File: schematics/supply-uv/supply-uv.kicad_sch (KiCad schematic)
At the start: 5 parts, among them J1 Conn_01x02_Pin, J3 Conn_01x01_Pin

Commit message: Found and fixed issues in schematics.
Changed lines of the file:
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@@
     (stroke (width 0) (type default))
+  )
+  (text_box "Known issues:\n- wrong place for R1-R3 (not a problem)\n- probably cooler required on QP1 (THIS IS PROBLEM!)\n- bad board layout near PFC GND"
+    (at 212.09 16.51 0) (size 68.58 48.26)
+    (stroke (width 0) (type default))
+    (fill (type none))
+    (effects (font (size 1.27 1.27)) (justify left top))
   )
   (text "Holes on board#2" (at 74.93 156.21 0)

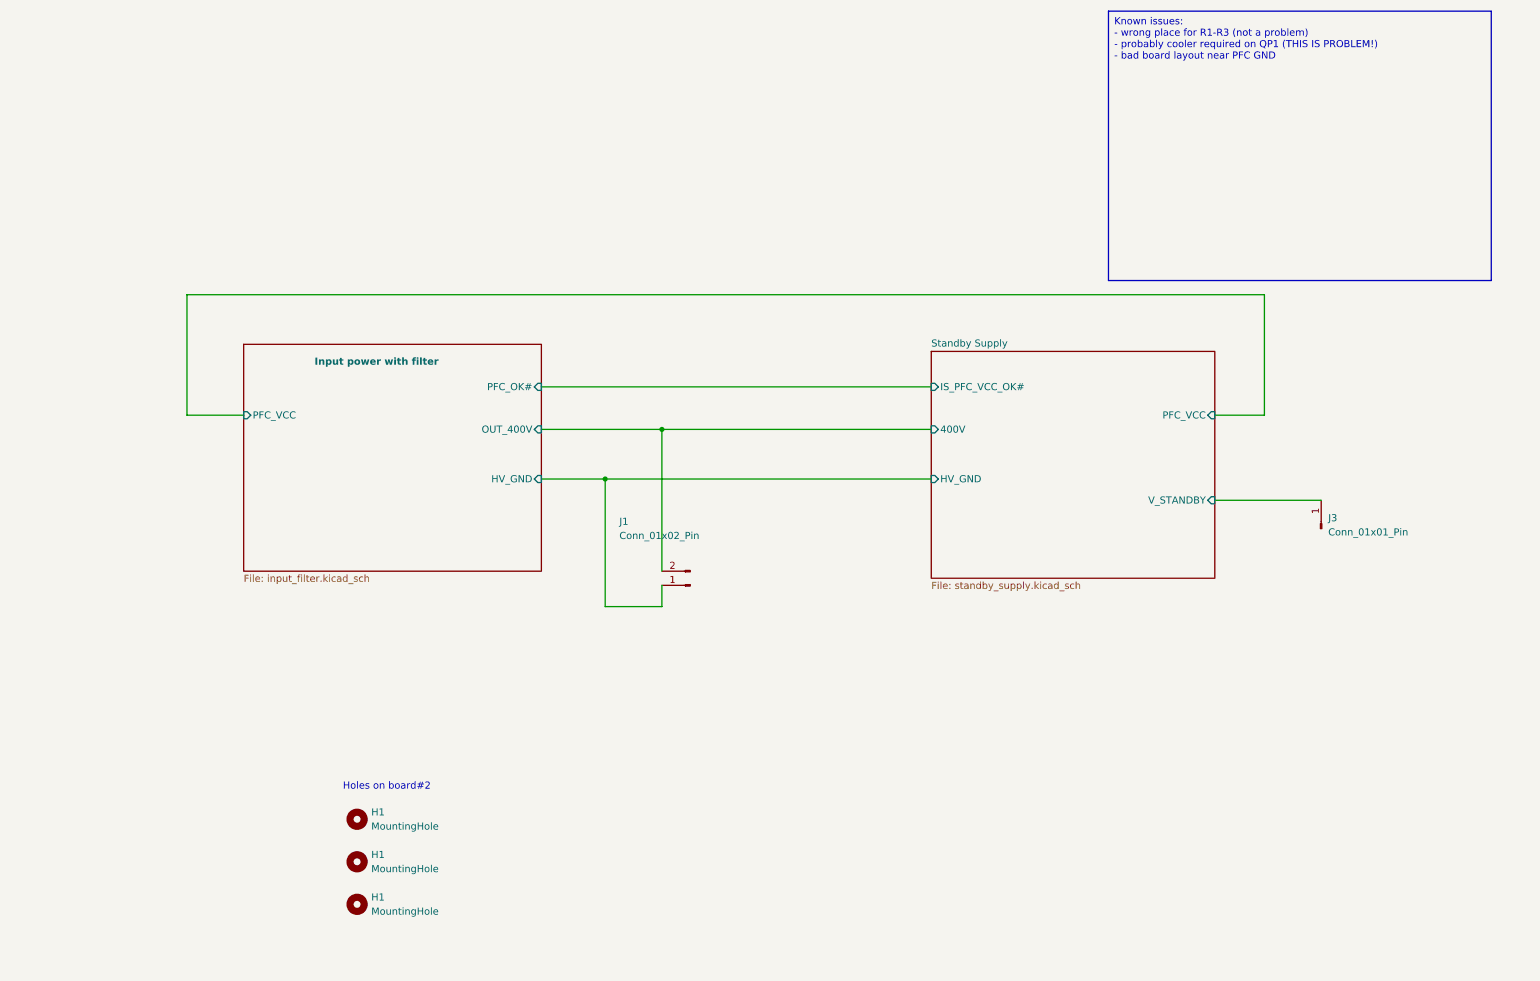
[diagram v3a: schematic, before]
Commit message: first schema version for board-uv
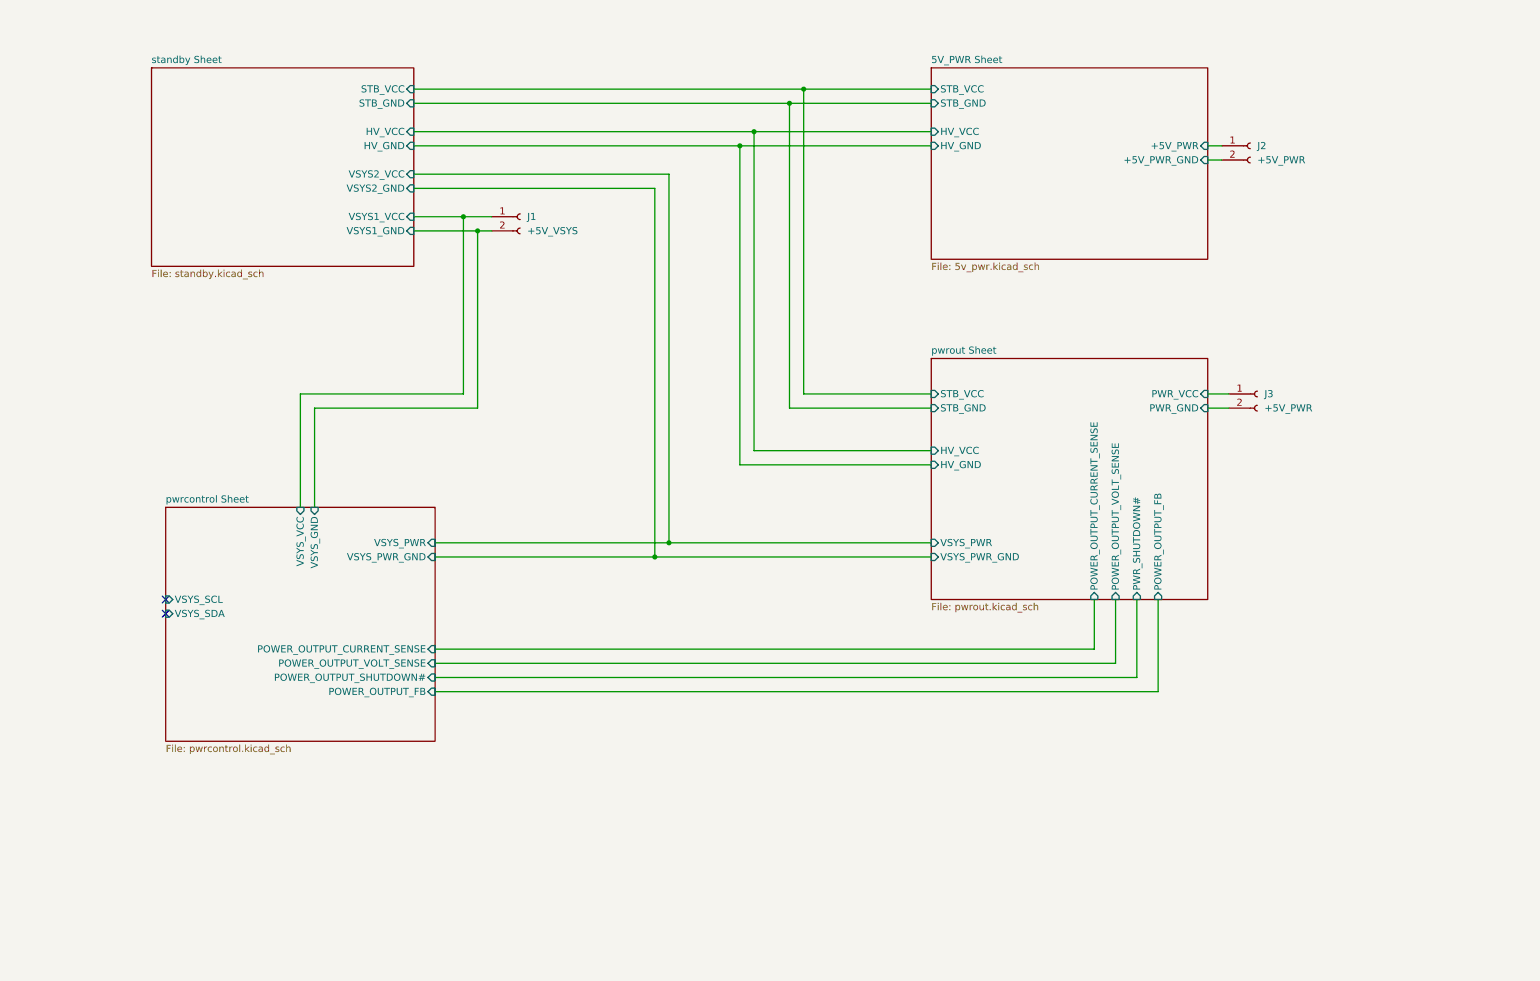
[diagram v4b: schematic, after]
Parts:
- removed H1 (x3): MountingHole, MountingHole:MountingHole_2.2mm_M2, symbol Mechanical:MountingHole
- removed J1: Conn_01x02_Pin, Connector_Wire:SolderWire-1.5sqmm_1x02_P6mm_D1.7mm_OD3mm, symbol Connector:Conn_01x02_Pin
- removed J3: Conn_01x01_Pin, Connector_Wire:SolderWire-1.5sqmm_1x01_D1.7mm_OD3.9mm, symbol Connector:Conn_01x01_Pin
- added J1: +5V_VSYS, symbol Connector:Conn_01x02_Socket
- added J2, J3: +5V_PWR, symbol Connector:Conn_01x02_Socket
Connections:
- new net 5V_PWR Sheet/+5V_PWR: J2.1 (Pin_1)
- new net 5V_PWR Sheet/+5V_PWR_GND: J2.2 (Pin_2)
- new net pwrcontrol Sheet/VSYS_GND: J1.2 (Pin_2)
- new net pwrcontrol Sheet/VSYS_VCC: J1.1 (Pin_1)
- new net pwrout Sheet/PWR_GND: J3.2 (Pin_2)
- new net pwrout Sheet/PWR_VCC: J3.1 (Pin_1)
- no-connect marks 0 -> 2
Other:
- removed sheet Input power with filter
- removed sheet Standby Supply
- added sheet 5V_PWR Sheet (5v_pwr.kicad_sch)
- added sheet pwrcontrol Sheet (pwrcontrol.kicad_sch)
- added sheet pwrout Sheet (pwrout.kicad_sch)
- added sheet standby Sheet (standby.kicad_sch)
- note removed: "Holes on board#2"

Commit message: Board#1 schematics rewrited
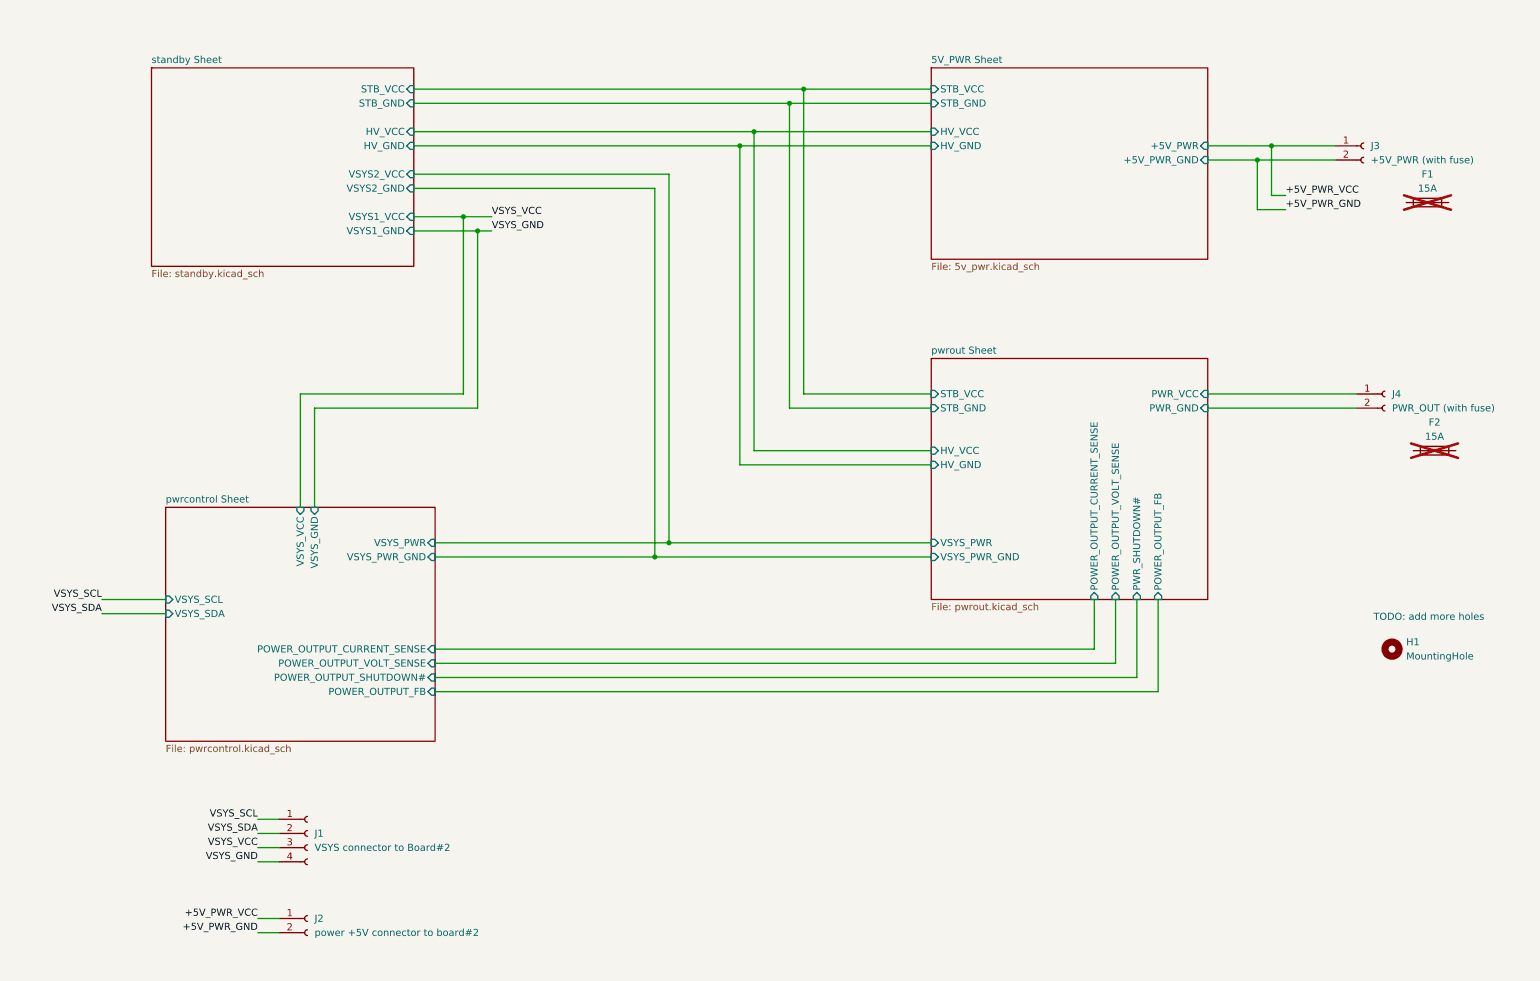
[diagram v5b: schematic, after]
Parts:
- removed J1: +5V_VSYS, symbol Connector:Conn_01x02_Socket
- removed J3: +5V_PWR, symbol Connector:Conn_01x02_Socket
- added F1, F2: 15A, symbol Device:Fuse
- added H1: MountingHole, MountingHole:MountingHole_2.2mm_M2, symbol Mechanical:MountingHole
- added J1: VSYS connector to Board#2, Connector_JST:JST_XH_B4B-XH-A_1x04_P2.50mm_Vertical, symbol Connector:Conn_01x04_Socket
- added J2: power +5V connector to board#2, Connector_Wire:SolderWire-1.5sqmm_1x02_P6mm_D1.7mm_OD3mm, symbol Connector:Conn_01x02_Socket
- added J4: PWR_OUT (with fuse), Connector_Wire:SolderWire-1.5sqmm_1x02_P6mm_D1.7mm_OD3mm, symbol Connector:Conn_01x02_Socket
- J3: renamed from J2; value +5V_PWR -> +5V_PWR (with fuse); footprint (none) -> Connector_Wire:SolderWire-1.5sqmm_1x02_P6mm_D1.7mm_OD3mm
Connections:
- net pwrout Sheet/PWR_GND: now also J4.2 (Pin_2)
- net pwrout Sheet/PWR_VCC: now also J4.1 (Pin_1)
- net 5V_PWR Sheet/+5V_PWR renamed +5V_PWR_VCC
- net +5V_PWR_VCC: now also J2.1 (Pin_1)
- net 5V_PWR Sheet/+5V_PWR_GND renamed +5V_PWR_GND
- net +5V_PWR_GND: now also J2.2 (Pin_2)
- new net VSYS_GND: J1.4 (Pin_4)
- new net VSYS_SCL: J1.1 (Pin_1)
- new net VSYS_SDA: J1.2 (Pin_2)
- new net VSYS_VCC: J1.3 (Pin_3)
- no-connect marks 2 -> 0
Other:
- note added: "TODO: add more holes"
- moved on the sheet: J3

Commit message: added some protection logic
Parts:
- added C1, C2: 100 nF, Capacitor_SMD:C_0603_1608Metric, symbol Device:C
- added U1: ISO1540, Package_SO:SOIC-8_3.9x4.9mm_P1.27mm, symbol Isolator:ISO1540
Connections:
- net VSYS_GND: now also C2.2, U1.5 (GND2)
- net VSYS_SCL: now also U1.6 (SCL2)
- net VSYS_SDA: now also U1.7 (SDA2)
- net VSYS_VCC: now also C2.1, U1.8 (VCC2)
- new net VSYS_PWR_GND: C1.2, U1.4 (GND1)
- new net VSYS_PWR_SCL: U1.3 (SCL1)
- new net VSYS_PWR_SDA: U1.2 (SDA1)
- new net VSYS_PWR_VCC: C1.1, U1.1 (VCC1)
- no-connect marks 0 -> 4
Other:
- sheet pwrcontrol Sheet ports: added SCL, SDA, VSYS_PWR_VCC; removed VSYS_GND, VSYS_PWR, VSYS_SCL, VSYS_SDA, VSYS_VCC
- sheet pwrout Sheet ports: added VSYS_PWR_VCC; removed VSYS_PWR
- moved on the sheet: J1, J2

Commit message: start board#1 tracing
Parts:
- added JP4: 5V_EN, Jumper:SolderJumper-2_P1.3mm_Open_TrianglePad1.0x1.5mm, symbol Jumper:SolderJumper_2_Open
- added JP5: PWR_EN, Jumper:SolderJumper-2_P1.3mm_Open_TrianglePad1.0x1.5mm, symbol Jumper:SolderJumper_2_Open
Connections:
- net 5V_PWR Sheet/STB_VCC: now also JP4.2 (B)
- new net pwrout Sheet/STB_VCC: JP5.2 (B)
- new net standby Sheet/STB_VCC: JP4.1 (A), JP5.1 (A)
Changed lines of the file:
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@@
 	)
 	(junction
-		(at 157.48 30.48)
+		(at 162.56 30.48)
 		(diameter 0)
 		(color 0 0 0 0)
@@
 	(wire
 		(pts
+			(xy 130.81 167.64) (xy 134.62 167.64)
+		)
+		(stroke
+			(width 0)
+			(type default)
+		)
+	)
+	(wire
+		(pts
 			(xy 148.59 38.1) (xy 180.34 38.1)
 		)
@@
 	(wire
 		(pts
+			(xy 130.81 165.1) (xy 134.62 165.1)
+		)
+		(stroke
+			(width 0)
+			(type default)
+		)
+	)
+	(wire
+		(pts
 			(xy 91.44 130.81) (xy 209.55 130.81)
 		)
@@
 	(wire
 		(pts
-			(xy 180.34 85.09) (xy 157.48 85.09)
+			(xy 176.53 85.09) (xy 180.34 85.09)
 		)
 		(stroke
@@
 	(wire
 		(pts
-			(xy 130.81 167.64) (xy 134.62 167.64)
-		)
-		(stroke
-			(width 0)
-			(type default)
-		)
-	)
-	(wire
-		(pts
 			(xy 130.81 170.18) (xy 134.62 170.18)
 		)
@@
 	(wire
 		(pts
-			(xy 157.48 30.48) (xy 180.34 30.48)
-		)
-		(stroke
-			(width 0)
-			(type default)
-		)
-	)
-	(wire
-		(pts
 			(xy 87.63 33.02) (xy 154.94 33.02)
 		)
@@
 	(wire
 		(pts
-			(xy 130.81 165.1) (xy 134.62 165.1)
-		)
-		(stroke
-			(width 0)
-			(type default)
-		)
-	)
-	(wire
-		(pts
 			(xy 213.36 133.35) (xy 213.36 121.92)
 		)
@@
 	(wire
 		(pts
+			(xy 162.56 30.48) (xy 167.64 30.48)
+		)
+		(stroke
+			(width 0)
+			(type default)
+		)
+	)
+	(wire
+		(pts
 			(xy 59.69 180.34) (xy 64.77 180.34)
 		)
@@
 	(wire
 		(pts
+			(xy 162.56 85.09) (xy 168.91 85.09)
+		)
+		(stroke
+			(width 0)
+			(type default)
+		)
+	)
+	(wire
+		(pts
 			(xy 238.76 52.07) (xy 238.76 43.18)
 		)
@@
 	(wire
 		(pts
-			(xy 87.63 30.48) (xy 157.48 30.48)
+			(xy 87.63 30.48) (xy 162.56 30.48)
 		)
 		(stroke
@@
 	(wire
 		(pts
-			(xy 157.48 85.09) (xy 157.48 30.48)
+			(xy 175.26 30.48) (xy 180.34 30.48)
+		)
+		(stroke
+			(width 0)
+			(type default)
+		)
+	)
+	(wire
+		(pts
+			(xy 162.56 85.09) (xy 162.56 30.48)
 		)
 		(stroke
@@
 			)
 			(justify right bottom)
+		)
+	)
+	(symbol
+		(lib_id "Jumper:SolderJumper_2_Open")
+		(at 171.45 30.48 0)
+		(unit 1)
+		(exclude_from_sim yes)
+		(in_bom no)
+		(on_board yes)
+		(dnp no)
+		(fields_autoplaced yes)
+		(property "Reference" "JP4"
+			(at 171.45 24.13 0)
+			(effects
+				(font
+					(size 1.27 1.27)
+				)
+			)
+		)
+		(property "Value" "5V_EN"
+			(at 171.45 26.67 0)
+			(effects
+				(font
+					(size 1.27 1.27)
+				)
+			)
+		)
+		(property "Footprint" "Jumper:SolderJumper-2_P1.3mm_Open_TrianglePad1.0x1.5mm"
+			(at 171.45 30.48 0)
+			(effects
+				(font
+					(size 1.27 1.27)
+				)
+				(hide yes)
+			)
+		)
+		(property "Datasheet" "~"
+			(at 171.45 30.48 0)
+			(effects
+				(font
+					(size 1.27 1.27)
+				)
+				(hide yes)
+			)
+		)
+		(property "Description" "Solder Jumper, 2-pole, open"
+			(at 171.45 30.48 0)
+			(effects
+				(font
+					(size 1.27 1.27)
+				)
+				(hide yes)
+			)
+		)
+		(pin "1"
+		)
+		(pin "2"
+		)
+		(instances
+			(project ""
+				(path "/ef40850c-d0bf-4cba-961b-9aba418f8e73"
+					(reference "JP4")
+					(unit 1)
+				)
+			)
 		)
 	)
@@
 					(unit 1)
 				)
+			)
+		)
+	)
+	(symbol
+		(lib_id "Jumper:SolderJumper_2_Open")
+		(at 172.72 85.09 0)
+		(unit 1)
+		(exclude_from_sim yes)
+		(in_bom no)
+		(on_board yes)
+		(dnp no)
+		(fields_autoplaced yes)
+		(property "Reference" "JP5"
+			(at 172.72 78.74 0)
+			(effects
+				(font
+					(size 1.27 1.27)
+				)
+			)
+		)
+		(property "Value" "PWR_EN"
+			(at 172.72 81.28 0)
+			(effects
+				(font
+					(size 1.27 1.27)
+				)
+			)
+		)
+		(property "Footprint" "Jumper:SolderJumper-2_P1.3mm_Open_TrianglePad1.0x1.5mm"
+			(at 172.72 85.09 0)
+			(effects
+				(font
+					(size 1.27 1.27)
+				)
+				(hide yes)
+			)
+		)
+		(property "Datasheet" "~"
+			(at 172.72 85.09 0)
+			(effects
+				(font
+					(size 1.27 1.27)
+				)
+				(hide yes)
+			)
+		)
+		(property "Description" "Solder Jumper, 2-pole, open"
+			(at 172.72 85.09 0)
+			(effects
+				(font
+					(size 1.27 1.27)
+				)
+				(hide yes)
+			)
+		)
+		(pin "1"
+		)
+		(pin "2"
+		)
+		(instances
+			(project "supply-uv"
+				(path "/ef40850c-d0bf-4cba-961b-9aba418f8e73"
+					(reference "JP5")
+					(unit 1)
+				)

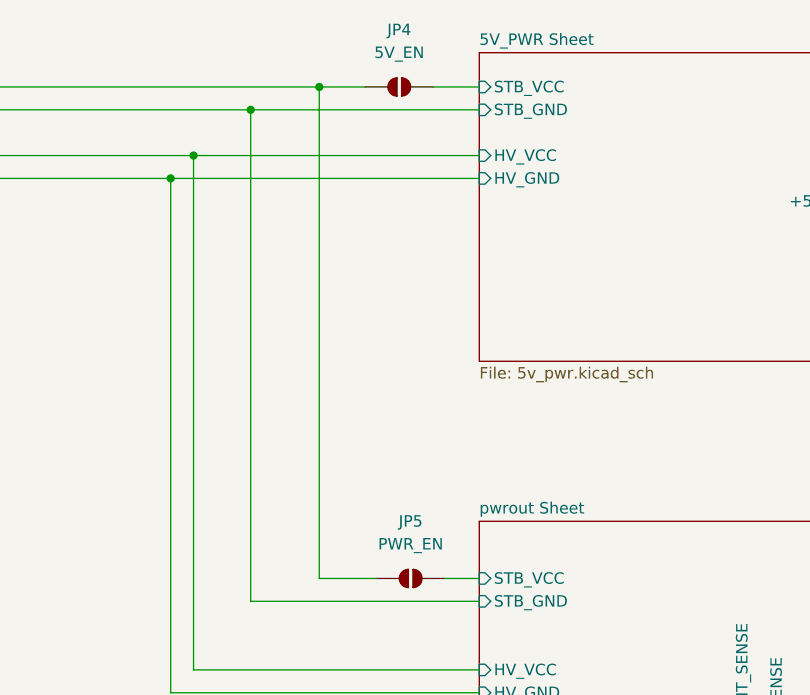
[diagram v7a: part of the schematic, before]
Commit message: First board routing completed. I will review it few days later and maybe optimize something, but base worki done
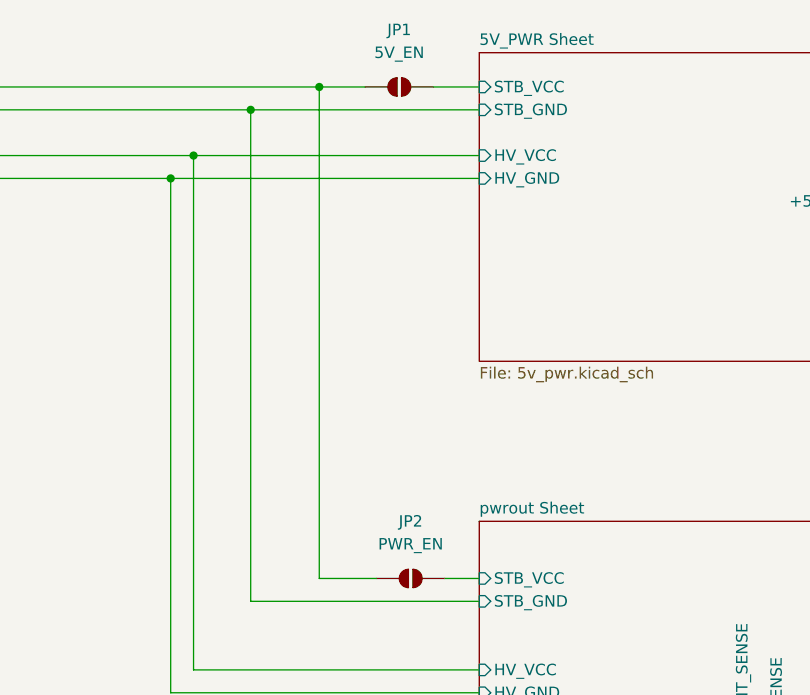
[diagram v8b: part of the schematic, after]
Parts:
- renumbered JP4 to JP1, JP5 to JP2
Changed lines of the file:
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@@
 		(dnp no)
 		(fields_autoplaced yes)
-		(property "Reference" "JP4"
+		(property "Reference" "JP1"
 			(at 171.45 24.13 0)
 			(effects
@@
 			(project ""
 				(path "/ef40850c-d0bf-4cba-961b-9aba418f8e73"
-					(reference "JP4")
+					(reference "JP1")
 					(unit 1)
 				)
@@
 		(dnp no)
 		(fields_autoplaced yes)
-		(property "Reference" "JP5"
+		(property "Reference" "JP2"
 			(at 172.72 78.74 0)
 			(effects
@@
 			(project "supply-uv"
 				(path "/ef40850c-d0bf-4cba-961b-9aba418f8e73"
-					(reference "JP5")
-					(unit 1)
-				)
+					(reference "JP2")
+					(unit 1)
+				)
